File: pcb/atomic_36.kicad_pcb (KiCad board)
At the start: 2 copper layers, 133.9 x 99 mm, 47 parts, among them J1 USB_C_12P

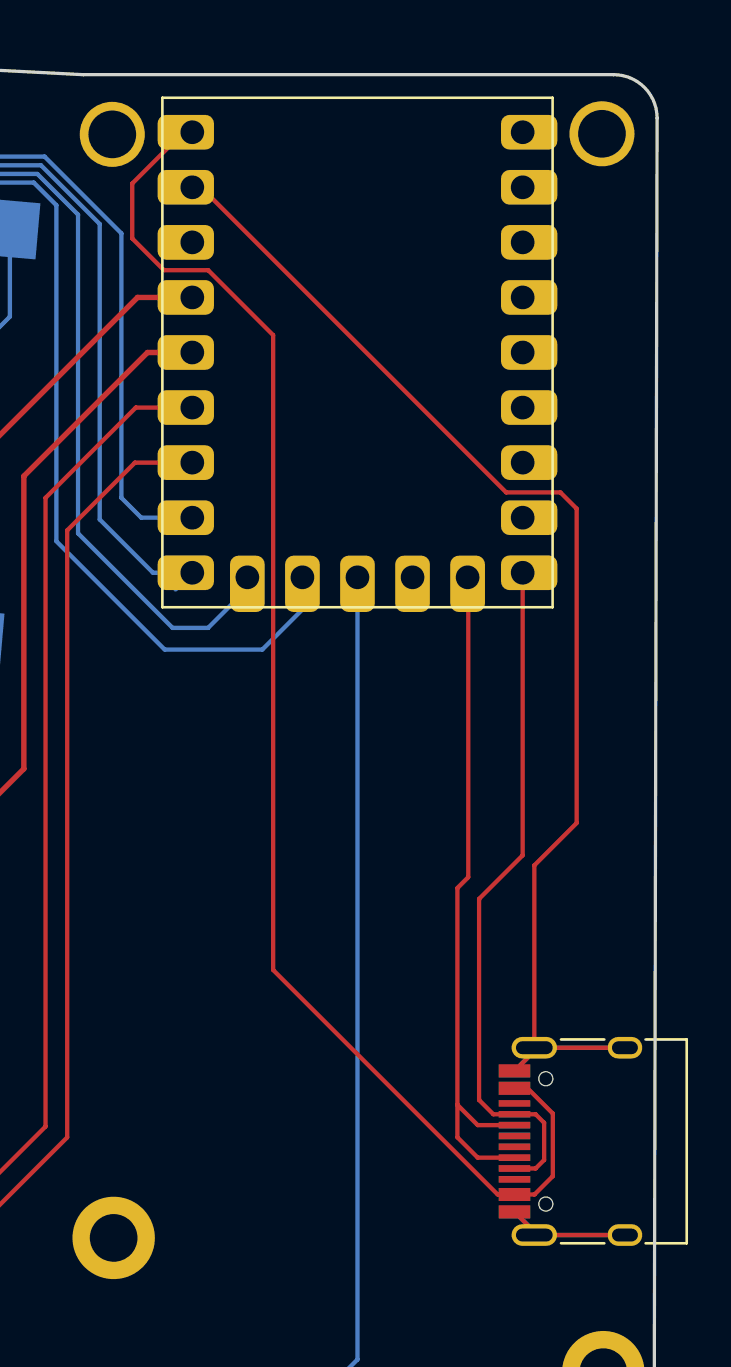
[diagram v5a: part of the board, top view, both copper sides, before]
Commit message: Route right (peripherial) USB C
GP8 and GP9 are used as TX and RX. The pins are from
left to right:

- GND
- P5V
- BLANK
- GP9 (RX)
- GP8 (TX)
- BLANK
- BLANK
- GP8 (TX)
- GP9 (RX)
- BLANK
- P5V
- GND

GP8/9 belong to UART1
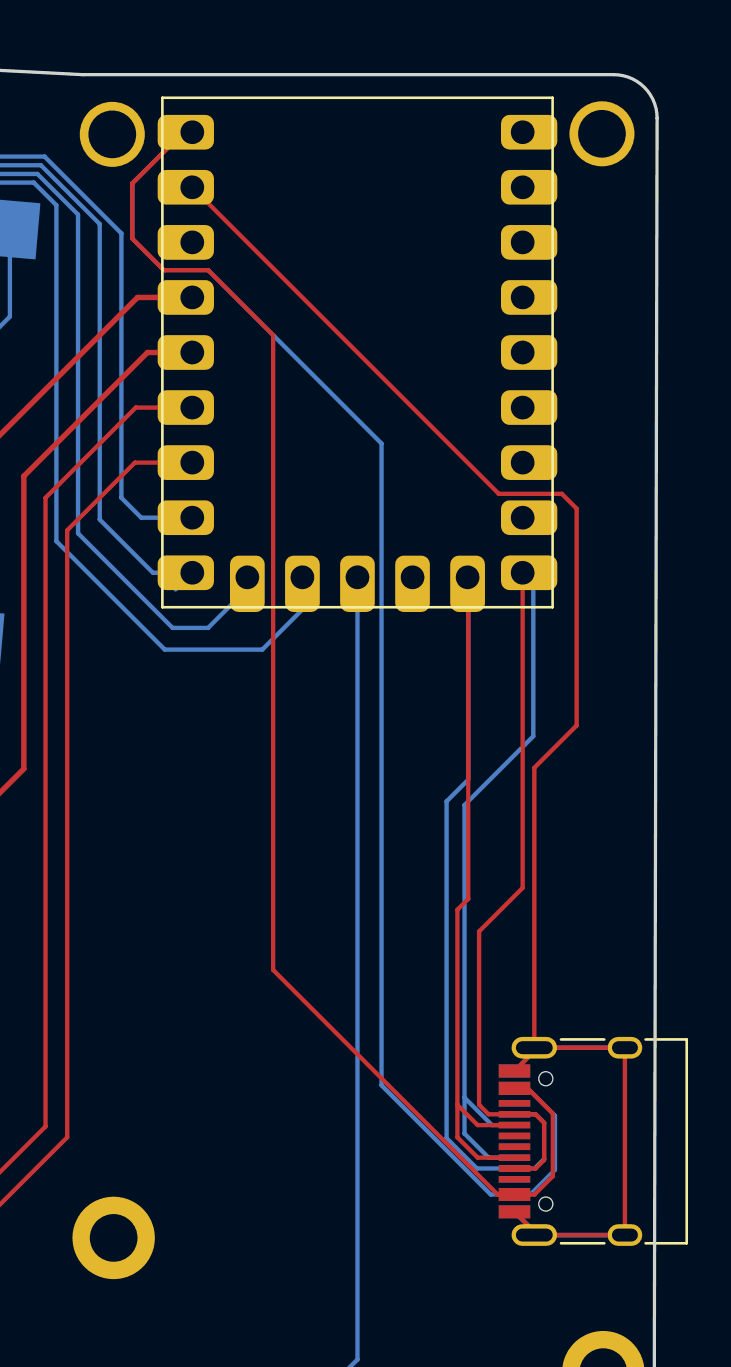
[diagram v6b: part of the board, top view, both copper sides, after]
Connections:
- J1 pad B11: VBUS -> P5V
- J1 pad B2: VBUS -> P5V
- J1 pad B4: (no net) -> GP9
- J1 pad B5: DM -> GP8
- J1 pad B6: DM -> (no net)
- J1 pad B7: DP -> (no net)
- J1 pad B8: DP -> GP8
- J1 pad B9: (no net) -> GP9
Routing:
- net P5V: track 66.6 -> 132.9 mm
- net GP9: track 32.1 -> 66.8 mm
- net GP8: track 31.8 -> 64.9 mm
- net GND: track 71.8 -> 86.2 mm

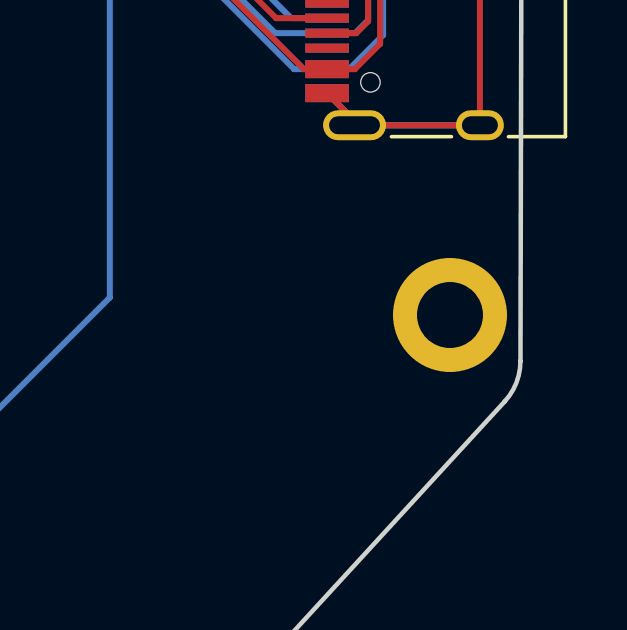
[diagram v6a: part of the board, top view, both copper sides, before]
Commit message: Fix DRC error, bottom right MCU cover hole issue
The bottom right MCU plated hole was too close to
the edge. I used a smaller plated hole (smaller in
that the plated ring diameter is smaller) from the
top of the MCU cover. I copied the X / Y positions
and tripled checked it. This passes DRC and should
still be in the exact same spot.
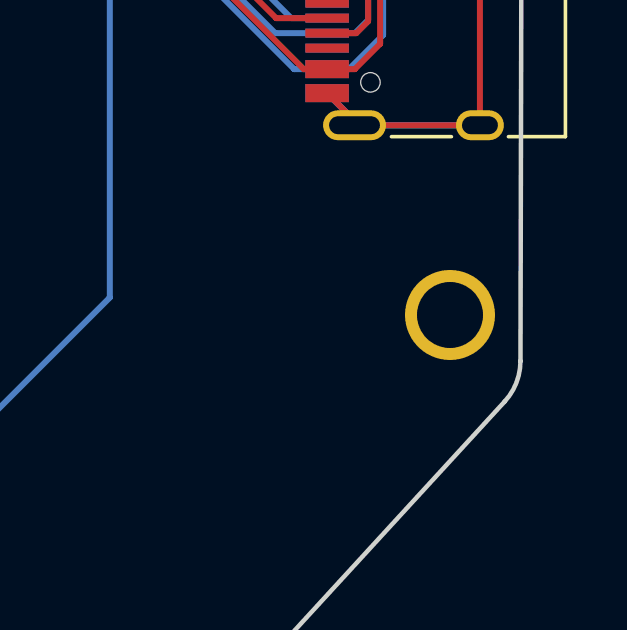
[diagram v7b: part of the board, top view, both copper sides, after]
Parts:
- removed H8: , ceoloide:mounting_hole_plated
- added H7: , ceoloide:mounting_hole_plated, F.Cu at (263.2, 155.8)
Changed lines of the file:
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@@
+	(footprint "ceoloide:mounting_hole_plated"
+		(layer "F.Cu")
+		(at 263.229204 155.830623 -5)
+		(property "Reference" "H7"
+			(at 0 3 355)
+			(layer "F.SilkS")
+			(hide yes)
+			(effects
+				(font
+					(size 1 1)
+					(thickness 0.15)
+				)
+			)
+		)
+		(property "Value" ""
+			(at 0 0 355)
+			(layer "F.Fab")
+			(effects
+				(font
+					(size 1.27 1.27)
+				)
+			)
+		)
+		(property "Datasheet" ""
+			(at 0 0 355)
+			(layer "F.Fab")
+			(hide yes)
+			(effects
+				(font
+					(size 1.27 1.27)
+				)
+			)
+		)
+		(property "Description" ""
+			(at 0 0 355)
+			(layer "F.Fab")
+			(hide yes)
+			(effects
+				(font
+					(size 1.27 1.27)
+				)
+			)
+		)
+		(duplicate_pad_numbers_are_jumpers no)
+		(fp_circle
+			(center 0 0)
+			(end -1.75 0)
+			(stroke
+				(width 0.05)
+				(type solid)
+			)
+			(fill no)
+			(layer "B.CrtYd")
+		)
+		(fp_circle
+			(center 0 0)
+			(end -1.75 0)
+			(stroke
+				(width 0.05)
+				(type solid)
+			)
+			(fill no)
+			(layer "F.CrtYd")
+		)
+		(pad "" thru_hole circle
+			(at 0 0 355)
+			(size 3 3)
+			(drill 2.2)
+			(layers "*.Cu" "*.Mask")
+			(remove_unused_layers no)
+		)
+		(embedded_fonts no)
+	)
 	(footprint "ceoloide:mounting_hole_plated"
 		(layer "F.Cu")
@@
 		)
 		(embedded_fonts no)
-	)
-	(footprint "ceoloide:mounting_hole_plated"
-		(layer "F.Cu")
-		(at 263.229204 155.830623 -5)
-		(property "Reference" "H8"
-			(at 0 3 355)
-			(layer "F.SilkS")
-			(hide yes)
-			(effects
-				(font
-					(size 1 1)
-					(thickness 0.15)
-				)
-			)
-		)
-		(property "Value" ""
-			(at 0 0 355)
-			(layer "F.Fab")
-			(effects
-				(font
-					(size 1.27 1.27)
-				)
-			)
-		)
-		(property "Datasheet" ""
-			(at 0 0 355)
-			(layer "F.Fab")
-			(hide yes)
-			(effects
-				(font
-					(size 1.27 1.27)
-				)
-			)
-		)
-		(property "Description" ""
-			(at 0 0 355)
-			(layer "F.Fab")
-			(hide yes)
-			(effects
-				(font
-					(size 1.27 1.27)
-				)
-			)
-		)
-		(duplicate_pad_numbers_are_jumpers no)
-		(fp_circle
-			(center 0 0)
-			(end -2.15 0)
-			(stroke
-				(width 0.05)
-				(type solid)
-			)
-			(fill no)
-			(layer "B.CrtYd")
-		)
-		(fp_circle
-			(center 0 0)
-			(end -2.15 0)
-			(stroke
-				(width 0.05)
-				(type solid)
-			)
-			(fill no)
-			(layer "F.CrtYd")
-		)
-		(pad "" thru_hole circle
-			(at 0 0 355)
-			(size 3.8 3.8)
-			(drill 2.2)
-			(layers "*.Cu" "*.Mask")
-			(remove_unused_layers no)
-		)
-		(embedded_fonts no)

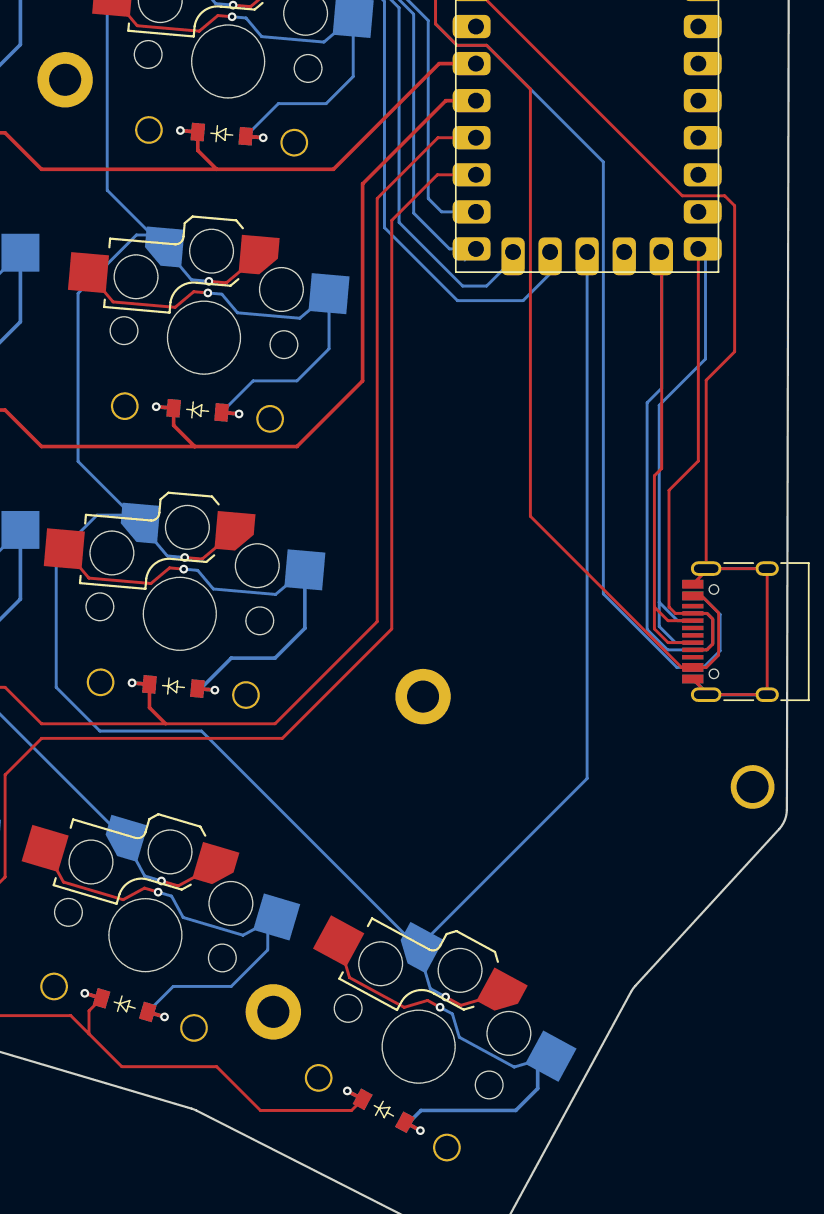
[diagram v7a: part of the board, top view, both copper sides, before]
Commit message: Tweak routes, add teardrops
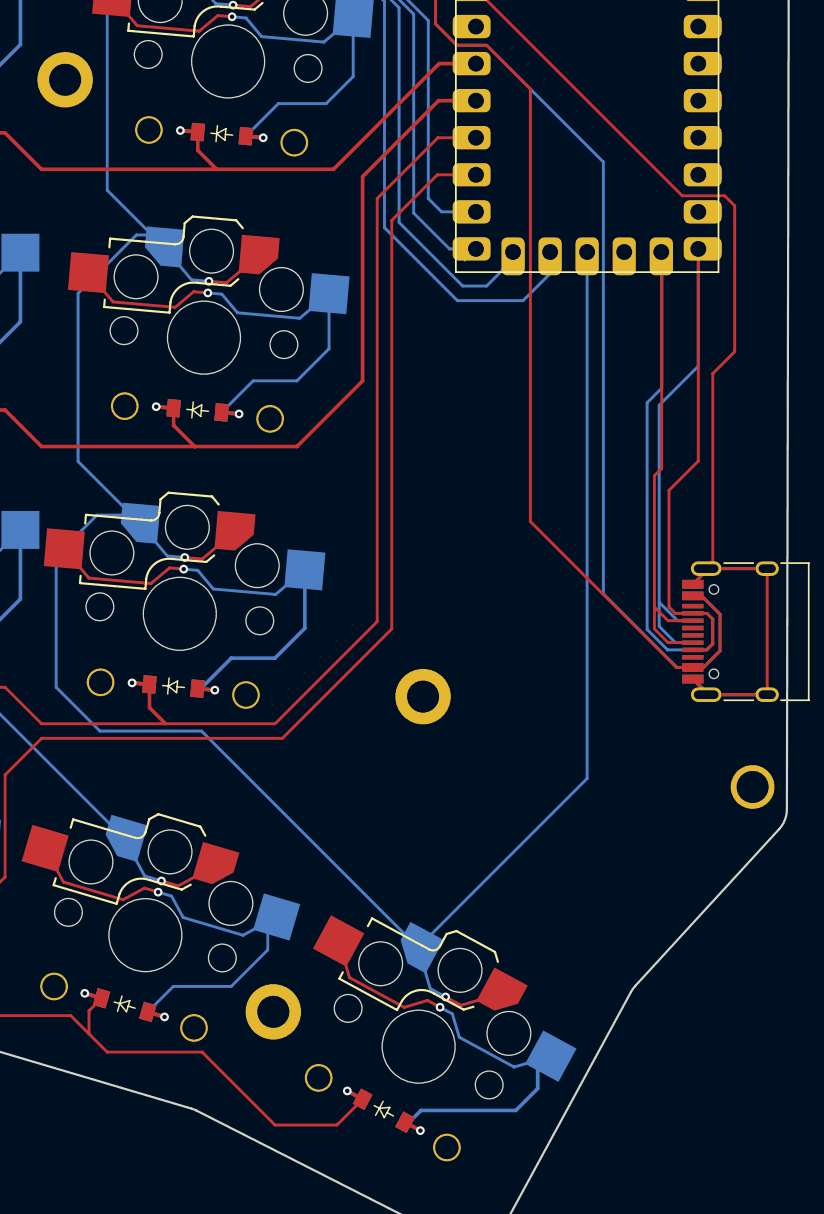
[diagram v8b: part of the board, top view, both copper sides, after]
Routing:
- net GP26: track 140.1 -> 141.0 mm
